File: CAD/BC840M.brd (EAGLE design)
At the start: 25.5 x 40 mm, 87 parts, among them J1 SM02B-SRSS-TB(LF)(SN), U2 BC840M, U3 LP5907MFX-3.3/NOPB, U4 LP5907MFX-3.3/NOPB, U5 ADS131M08IPBS, X1 ABM3B-8.000MHZ-B2-T, X2 FC-12M

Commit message: tweaks
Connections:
- new net VDDH: R2.2, R25.1, R28.1, R29.1, U2.A7
- net VDD: no longer R2.2, R25.1, R28.1, R29.1, U2.A7
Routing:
- net VDD: track 86.3 -> 46.3 mm
- net VDDH: track 0.00 -> 39.9 mm
- net GND: track 161.1 -> 165.6 mm
- net P113: track 22.0 -> 22.8 mm
- net CUR_DETECT: track 29.2 -> 28.3 mm
- net RESET: track 30.7 -> 30.0 mm

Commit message: Update BC840M.brd
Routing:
- net GND: track 165.6 -> 177.9 mm
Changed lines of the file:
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@@
 <wire x1="32.778640625" y1="48.306040625" x2="32.778640625" y2="47.652940625" width="0.1524" layer="16"/>
 <wire x1="32.778640625" y1="47.652940625" x2="35.054540625" y2="47.652940625" width="0.1524" layer="16"/>
+<wire x1="29.910021875" y1="42.274640625" x2="31.122721875" y2="43.487340625" width="0.1524" layer="16"/>
+<wire x1="31.122721875" y1="43.487340625" x2="32.699959375" y2="43.487340625" width="0.1524" layer="16"/>
+<wire x1="33.910021875" y1="44.674640625" x2="32.722721875" y2="43.487340625" width="0.1524" layer="16"/>
+<wire x1="32.722721875" y1="43.487340625" x2="32.699959375" y2="43.487340625" width="0.1524" layer="16"/>
+<wire x1="25.945503125" y1="31.252315625" x2="27.0635375" y2="31.252315625" width="0.1524" layer="16"/>
+<wire x1="20.3454" y1="31.7246" x2="21.2806375" y2="30.7893625" width="0.1524" layer="16"/>
+<wire x1="21.2806375" y1="30.7893625" x2="25.48255" y2="30.7893625" width="0.1524" layer="16"/>
+<wire x1="25.48255" y1="30.7893625" x2="25.945503125" y2="31.252315625" width="0.1524" layer="16"/>
 <wire x1="27.559" y1="60.2964" x2="27.559" y2="61.1092" width="0" layer="19" extent="1-1"/>
 <wire x1="28.3464" y1="60.2964" x2="28.3464" y2="59.509" width="0" layer="19" extent="1-1"/>
@@
 <wire x1="14.302740625" y1="34.2392" x2="15.76578125" y2="33.830259375" width="0" layer="19" extent="1-1"/>
 <wire x1="20.3454" y1="31.7246" x2="18.7208" y2="31.765859375" width="0" layer="19" extent="1-1"/>
-<wire x1="27.072778125" y1="32.0904625" x2="25.887778125" y2="32.731340625" width="0" layer="19" extent="1-1"/>
 <wire x1="28.072778125" y1="32.0904625" x2="27.072778125" y2="32.0904625" width="0" layer="19" extent="1-1"/>
 <wire x1="13.6118625" y1="35.699" x2="14.302740625" y2="34.2392" width="0" layer="19" extent="1-1"/>
@@
 <wire x1="28.724978125" y1="48.97120625" x2="31.278640625" y2="48.306040625" width="0" layer="19" extent="1-16"/>
 <wire x1="27.4828" y1="51.4269" x2="26.2609375" y2="49.2353625" width="0" layer="19" extent="1-1"/>
+<wire x1="35.676840625" y1="42.659178125" x2="33.910021875" y2="44.674640625" width="0" layer="19" extent="16-16"/>
 <wire x1="27.739459375" y1="55.83681875" x2="30.56901875" y2="56.3397375" width="0" layer="19" extent="1-16"/>
 <wire x1="26.9162625" y1="55.80888125" x2="27.739459375" y2="55.83681875" width="0" layer="19" extent="1-1"/>
 <wire x1="26.733378125" y1="54.480465625" x2="26.9162625" y2="55.80888125" width="0" layer="19" extent="1-1"/>
-<wire x1="32.699959375" y1="43.487340625" x2="29.910021875" y2="42.274640625" width="0" layer="19" extent="16-16"/>
-<wire x1="33.910021875" y1="44.674640625" x2="32.699959375" y2="43.487340625" width="0" layer="19" extent="16-16"/>
-<wire x1="35.676840625" y1="42.659178125" x2="33.910021875" y2="44.674640625" width="0" layer="19" extent="16-16"/>
 <wire x1="35.9156" y1="39.8018" x2="35.676840625" y2="42.659178125" width="0" layer="19" extent="16-16"/>
 <wire x1="34.2395" y1="39.237921875" x2="35.9156" y2="39.8018" width="0" layer="19" extent="1-1"/>

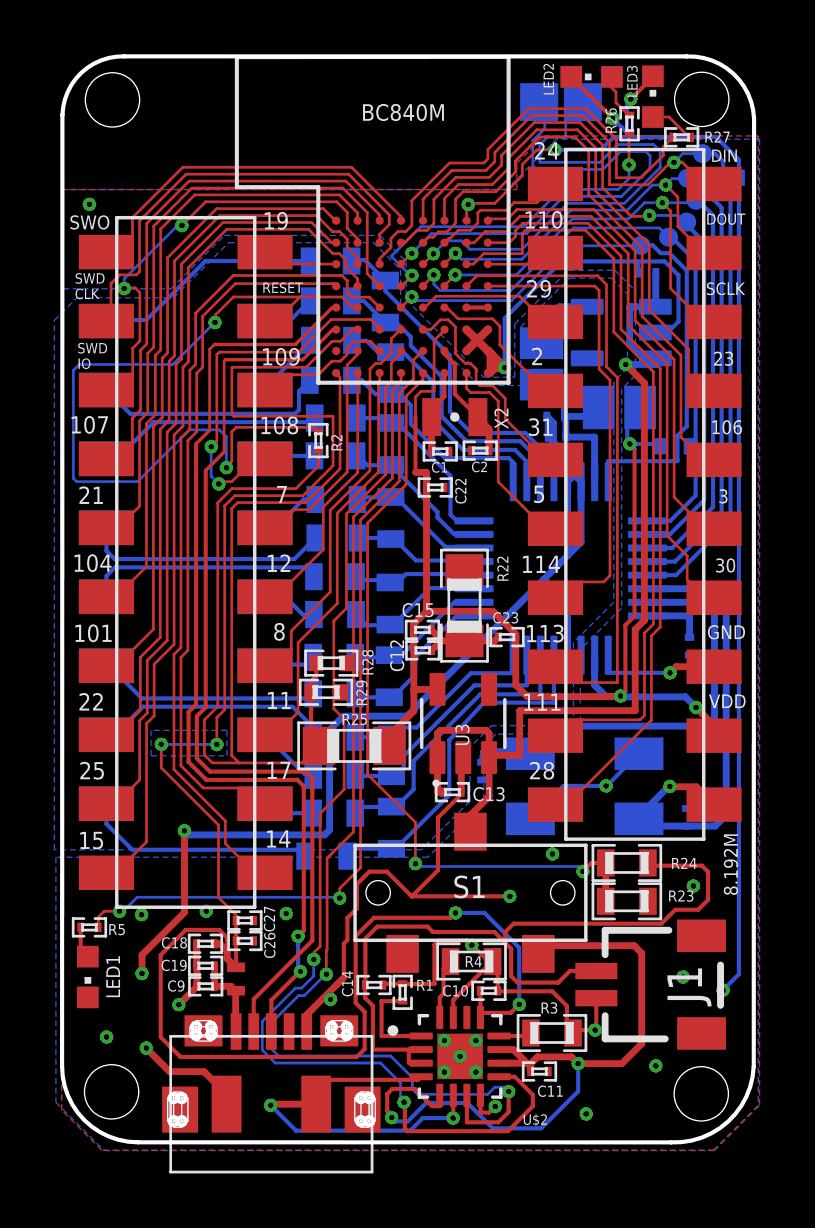
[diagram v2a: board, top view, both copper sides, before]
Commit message: added TVS diodes
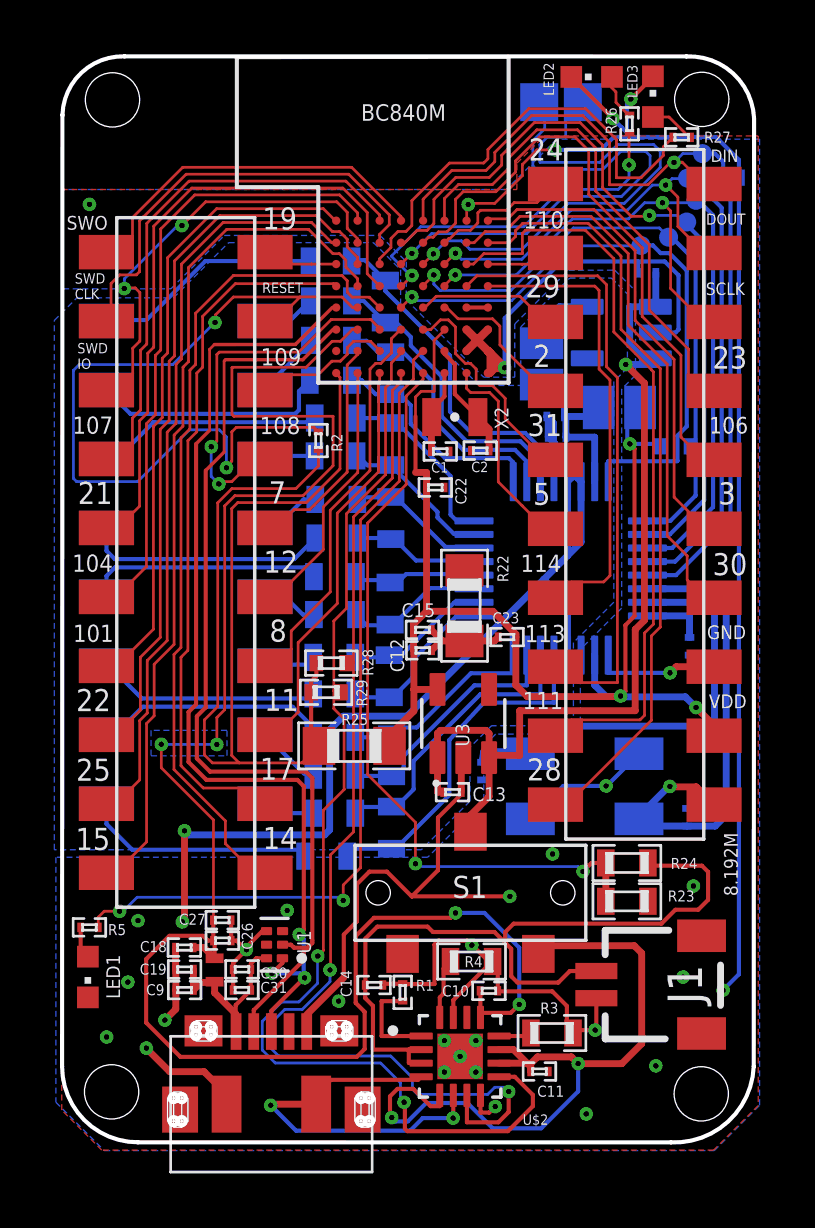
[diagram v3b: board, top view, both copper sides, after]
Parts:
- added C30: 0.1uF, standardparts:0201
- added C31: 10uF, standardparts:0201
- added U1: TPD4S012DRYR, TPD4S012DRYR:PSON50P145X100X60-6N
- moved U$3 0.85 mm to (18.3, 36.7)
- moved C27 0.83 mm to (18.6, 38.5)
- moved C26 0.83 mm to (18.6, 37.8)
- moved C9 0.79 mm to (17.2, 36.0)
- moved C18 0.79 mm to (17.2, 37.5)
- moved C19 0.79 mm to (17.2, 36.7)
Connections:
- net +5V: now also C30.2, C31.2, U1.6
- net D+: now also U1.1
- net D-: now also U1.2
- net GND: now also C30.1, C31.1, U1.4
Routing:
- net +5V: track 3.32 -> 6.76 mm
- net GND: track 177.9 -> 180.1 mm, vias 29 -> 30
- net D+: track 35.0 -> 37.1 mm, vias 2 -> 3
- net +5V_ISO: track 69.3 -> 67.7 mm
- net D-: track 34.4 -> 35.4 mm

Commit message: push
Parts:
- C16, C17, C20, C21, C24, C25, C28, C29: value 10pF -> 100pF
- R10, R11, R12, R13, R14, R15, R16, R17, R18, R19, R20, R21, R6, R7, R8, R9: value 10MOhm -> 1MOhm
- renumbered U$1 to U7, U$2 to U6, U$3 to I1

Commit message: latest
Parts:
- C15, C31: device standardparts:0201 -> standardparts:0402
- moved I1 0.62 mm to (17.7, 36.7)
- moved C9 0.56 mm to (16.6, 36.0)
- moved C18 0.56 mm to (16.6, 37.4)
- moved C19 0.55 mm to (16.6, 36.7)
- moved C30 0.53 mm to (18.9, 37.1)
- moved C12 0.39 mm to (25.6, 48.4)
- moved C31 0.37 mm to (19.0, 36.2)
- moved C15 0.33 mm to (25.6, 49.2)
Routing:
- net +5V: track 6.76 -> 7.82 mm
- net VDD: track 46.3 -> 47.2 mm

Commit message: edits and CAM
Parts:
- J1: value SM02B-SRSS-TB(LF)(SN) -> S2B-PH-SM4-TB(LF)(SN); device SM02B-SRSS-TB_LF__SN_:SM02B-SRSS-TB(LF)(SN) -> S2B-PH-SM4-TB_LF__SN_:JST_S2B-PH-SM4-TB(LF)(SN)
- moved R31 0.50 mm to (35.3, 55.5)
- moved SJ1 0.37 mm to (33.2, 57.1)
- moved I1 0.35 mm to (17.4, 37.0)
- moved C9 0.31 mm to (16.3, 36.0)
- moved C19 0.30 mm to (16.3, 36.7)
- moved C18 0.30 mm to (16.3, 37.4)
- moved C15 0.07 mm to (25.6, 49.3)
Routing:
- net VDD: track 47.2 -> 51.3 mm
- net GND: track 180.3 -> 182.8 mm
- net BAT: track 29.0 -> 31.4 mm
- net +5V: track 7.82 -> 8.64 mm
- net +5V_ISO: track 68.1 -> 68.7 mm

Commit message: fix
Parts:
- J1: value S2B-PH-SM4-TB(LF)(SN) -> SM02B-SRSS-TB(LF)(SN); device S2B-PH-SM4-TB_LF__SN_:JST_S2B-PH-SM4-TB(LF)(SN) -> SM02B-SRSS-TB_LF__SN_:SM02B-SRSS-TB(LF)(SN)
- moved J1 0.22 mm to (34.5, 36.1)
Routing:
- net BAT: track 31.4 -> 29.3 mm
- net GND: track 182.8 -> 181.0 mm
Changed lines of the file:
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@@
 <attribute name="VALUE" x="29.217515625" y="30.905684375" size="0.381" layer="27" rot="R180" align="top-left"/>
-</element>
-<element name="J1" library="S2B-PH-SM4-TB_LF__SN_" package="JST_S2B-PH-SM4-TB(LF)(SN)" value="S2B-PH-SM4-TB(LF)(SN)" x="34.3154" y="36.1696" smashed="yes" rot="R90">
-<attribute name="AVAILABILITY" value="In Stock" x="34.3154" y="36.1696" size="1.778" layer="27" rot="R90" display="off"/>
-<attribute name="DESCRIPTION" value=" Connector Header Surface Mount, Right Angle 2 position 0.079 (2.00mm) " x="34.3154" y="36.1696" size="1.778" layer="27" rot="R90" display="off"/>
-<attribute name="MF" value="JST Sales" x="34.3154" y="36.1696" size="1.778" layer="27" rot="R90" display="off"/>
-<attribute name="MP" value="S2B-PH-SM4-TB (LF)(SN)" x="34.3154" y="36.1696" size="1.778" layer="27" rot="R90" display="off"/>
-<attribute name="NAME" x="35.5953625" y="36.17834375" size="1.27315" layer="25" rot="R90" align="center"/>
-<attribute name="PACKAGE" value="None" x="34.3154" y="36.1696" size="1.778" layer="27" rot="R90" display="off"/>
-<attribute name="PRICE" value="None" x="34.3154" y="36.1696" size="1.778" layer="27" rot="R90" display="off"/>
-<attribute name="VALUE" x="37.632515625" y="35.9325375" size="0.4064" layer="27" rot="R270" align="center"/>
 </element>
 <element name="JP1" library="pinhead+" package="2X08_SMT" value="" x="17.2186625" y="51.7245625" smashed="yes" rot="MR90">
@@
 <attribute name="NAME" x="20.091390625" y="35.824153125" size="0.4064" layer="25" font="vector"/>
 <attribute name="VALUE" x="18.356575" y="35.298375" size="0.4064" layer="27" font="vector"/>
+</element>
+<element name="J1" library="SM02B-SRSS-TB_LF__SN_" package="SM02B-SRSS-TB(LF)(SN)" value="SM02B-SRSS-TB(LF)(SN)" x="34.533840625" y="36.14928125" smashed="yes" rot="R90">
+<attribute name="AVAILABILITY" value="In Stock" x="34.533840625" y="36.14928125" size="1.778" layer="27" rot="R90" display="off"/>
+<attribute name="DESCRIPTION" value=" Connector Header Surface Mount, Right Angle 2 position 0.039 (1.00mm) " x="34.533840625" y="36.14928125" size="1.778" layer="27" rot="R90" display="off"/>
+<attribute name="MF" value="JST Sales" x="34.533840625" y="36.14928125" size="1.778" layer="27" rot="R90" display="off"/>
+<attribute name="MP" value="SM02B-SRSS-TB(LF)(SN)" x="34.533840625" y="36.14928125" size="1.778" layer="27" rot="R90" display="off"/>
+<attribute name="NAME" x="34.924803125" y="35.802425" size="1.27315" layer="25" rot="R90" align="center"/>
+<attribute name="PACKAGE" value="None" x="34.533840625" y="36.14928125" size="1.778" layer="27" rot="R90" display="off"/>
+<attribute name="PRICE" value="None" x="34.533840625" y="36.14928125" size="1.778" layer="27" rot="R90" display="off"/>
+<attribute name="VALUE" x="34.925125" y="35.80214375" size="1.27416875" layer="27" rot="R90" align="center"/>
 </element>
 </elements>
@@
 <contactref element="U7" pad="MP1"/>
 <contactref element="U7" pad="MP2"/>
-<contactref element="J1" pad="1"/>
 <contactref element="R3" pad="1"/>
 <contactref element="R4" pad="1"/>
@@
 <wire x1="15.9945" y1="37.442134375" x2="15.9945" y2="36.7004625" width="0.254" layer="1"/>
 <wire x1="15.99704375" y1="36.69791875" x2="15.9945" y2="36.7004625" width="0.254" layer="1"/>
-<wire x1="15.981809375" y1="35.95115625" x2="16.29676875" y2="35.636196875" width="0.254" layer="1"/>
-<wire x1="16.29676875" y1="35.636196875" x2="16.29676875" y2="35.011246875" width="0.254" layer="1"/>
+<wire x1="16.29676875" y1="35.438075" x2="15.981809375" y2="35.753034375" width="0.254" layer="1"/>
+<wire x1="15.981809375" y1="35.95115625" x2="15.981809375" y2="35.753034375" width="0.254" layer="1"/>
+<wire x1="16.29676875" y1="35.438075" x2="16.29676875" y2="35.011246875" width="0.254" layer="1"/>
 <wire x1="16.446509375" y1="34.86150625" x2="16.29676875" y2="35.011246875" width="0.254" layer="1"/>
 <contactref element="U6" pad="15"/>
@@
 <wire x1="31.255003125" y1="35.38395625" x2="31.255003125" y2="34.61258125" width="0.1524" layer="1"/>
 <wire x1="31.4810625" y1="34.386521875" x2="31.255003125" y2="34.61258125" width="0.1524" layer="1"/>
-<wire x1="31.255003125" y1="35.38395625" x2="30.717340625" y2="35.92161875" width="0.1524" layer="1"/>
+<wire x1="31.255003125" y1="35.38395625" x2="31.164290625" y2="35.47466875" width="0.1524" layer="1"/>
+<wire x1="31.164290625" y1="35.47466875" x2="30.717340625" y2="35.92161875" width="0.1524" layer="1"/>
 <wire x1="31.4810625" y1="34.386521875" x2="31.587740625" y2="34.4932" width="0.1524" layer="1"/>
 <wire x1="31.587740625" y1="34.4932" x2="32.2961" y2="34.4932" width="0.1524" layer="1"/>
 <wire x1="32.2961" y1="34.4932" x2="32.3404" y2="34.5375" width="0.1524" layer="1"/>
-<wire x1="32.3404" y1="34.5375" x2="34.3154" y2="37.1696" width="0.1524" layer="1"/>
 <wire x1="28.963621875" y1="58.88989375" x2="28.963621875" y2="60.712190625" width="0.1524" layer="16"/>
 <wire x1="28.963621875" y1="60.712190625" x2="31.0580125" y2="62.80658125" width="0.1524" layer="16"/>
@@
 <wire x1="26.130334375" y1="49.283621875" x2="26.3437" y2="49.283621875" width="0.254" layer="1"/>
 <wire x1="26.413815625" y1="49.21350625" x2="26.413815625" y2="48.8269" width="0.254" layer="1"/>
+<contactref element="J1" pad="1"/>
+<wire x1="31.164290625" y1="35.47466875" x2="32.384228125" y2="35.47466875" width="0.1524" layer="1"/>
+<wire x1="32.384228125" y1="35.47466875" x2="32.558840625" y2="35.64928125" width="0.1524" layer="1"/>
 <wire x1="27.559" y1="60.2964" x2="27.559" y2="61.1092" width="0" layer="19" extent="1-1"/>
 <wire x1="28.3464" y1="60.2964" x2="28.3464" y2="59.509" width="0" layer="19" extent="1-1"/>
@@
 <wire x1="30.57131875" y1="32.9692" x2="28.61564375" y2="31.67634375" width="0" layer="19" extent="1-1"/>
 <wire x1="31.4810625" y1="34.386521875" x2="30.57131875" y2="32.9692" width="0" layer="19" extent="1-1"/>
-<wire x1="35.5346" y1="36.449" x2="34.3154" y2="37.1696" width="0" layer="19" extent="1-1"/>
-<wire x1="37.0078" y1="35.9664" x2="35.5346" y2="36.449" width="0" layer="19" extent="1-1"/>
 <wire x1="22.8473" y1="35.56" x2="24.477859375" y2="36.154359375" width="0" layer="19" extent="1-1"/>
 <wire x1="21.6708" y1="34.440859375" x2="22.8473" y2="35.56" width="0" layer="19" extent="1-1"/>
 <wire x1="28.125421875" y1="43.708440625" x2="27.3658375" y2="43.258740625" width="0" layer="19" extent="1-16"/>
-<wire x1="34.2395" y1="39.237921875" x2="34.3154" y2="37.1696" width="0" layer="19" extent="1-1"/>
-<wire x1="35.9156" y1="39.8018" x2="34.2395" y2="39.237921875" width="0" layer="19" extent="1-1"/>
 <wire x1="31.968440625" y1="31.4071" x2="30.57131875" y2="32.9692" width="0" layer="19" extent="1-1"/>
 <wire x1="30.72638125" y1="40.980359375" x2="29.15411875" y2="39.4208" width="0" layer="19" extent="1-1"/>
 <wire x1="29.910021875" y1="42.274640625" x2="30.72638125" y2="40.980359375" width="0" layer="19" extent="16-16"/>
-<wire x1="34.5313" y1="33.17748125" x2="32.2961" y2="34.4932" width="0" layer="19" extent="1-1"/>
+<wire x1="34.5313" y1="33.17748125" x2="32.3404" y2="34.5375" width="0" layer="19" extent="1-1"/>
 <wire x1="28.724978125" y1="48.97120625" x2="31.278640625" y2="48.306040625" width="0" layer="19" extent="1-16"/>
 <wire x1="27.4828" y1="51.4269" x2="26.130334375" y2="49.283621875" width="0" layer="19" extent="1-1"/>
@@
 <wire x1="26.9162625" y1="55.80888125" x2="27.739459375" y2="55.83681875" width="0" layer="19" extent="1-1"/>
 <wire x1="26.733378125" y1="54.480465625" x2="26.9162625" y2="55.80888125" width="0" layer="19" extent="1-1"/>
+<wire x1="35.9156" y1="39.8018" x2="35.676840625" y2="42.659178125" width="0" layer="19" extent="16-16"/>
+<wire x1="34.2395" y1="39.237921875" x2="35.9156" y2="39.8018" width="0" layer="19" extent="1-1"/>
+<wire x1="35.5346" y1="36.449" x2="32.558840625" y2="35.64928125" width="0" layer="19" extent="1-1"/>
+<wire x1="37.0078" y1="35.9664" x2="35.5346" y2="36.449" width="0" layer="19" extent="1-1"/>
 <wire x1="13.67028125" y1="64.907159375" x2="27.559" y2="64.3096" width="0" layer="19" extent="1-1"/>
 </signal>
@@
 <contactref element="C14" pad="2"/>
 <contactref element="U6" pad="2"/>
-<contactref element="J1" pad="2"/>
-<wire x1="34.3154" y1="35.1696" x2="31.3650375" y2="36.6696" width="0.1524" layer="1"/>
-<wire x1="31.3650375" y1="36.6696" x2="30.94085625" y2="36.24541875" width="0.1524" layer="1"/>
+<wire x1="30.94085625" y1="36.24541875" x2="31.3650375" y2="36.6696" width="0.1524" layer="1"/>
 <wire x1="30.94085625" y1="36.24541875" x2="29.436440625" y2="36.24541875" width="0.1524" layer="1"/>
 <wire x1="29.436440625" y1="36.24541875" x2="29.20491875" y2="36.476940625" width="0.1524" layer="1"/>
@@
 <wire x1="26.124053125" y1="38.305740625" x2="26.32201875" y2="38.107775" width="0.1524" layer="1"/>
 <wire x1="24.274778125" y1="38.305740625" x2="26.124053125" y2="38.305740625" width="0.1524" layer="1"/>
+<contactref element="J1" pad="2"/>
+<wire x1="31.3650375" y1="36.6696" x2="32.538521875" y2="36.6696" width="0.1524" layer="1"/>
+<wire x1="32.538521875" y1="36.6696" x2="32.558840625" y2="36.64928125" width="0.1524" layer="1"/>
 </signal>
 <signal name="0PIN">

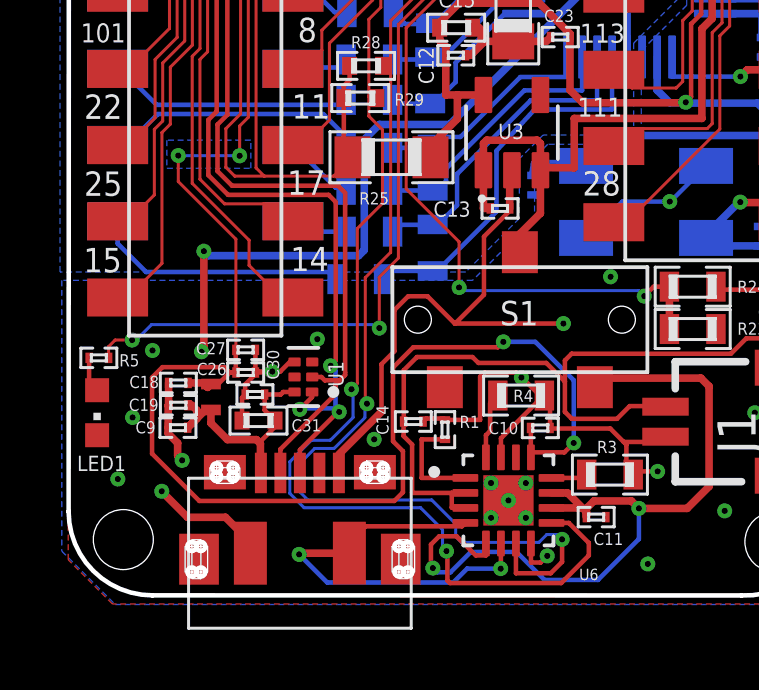
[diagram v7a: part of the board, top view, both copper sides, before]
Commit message: fix holes for microusb
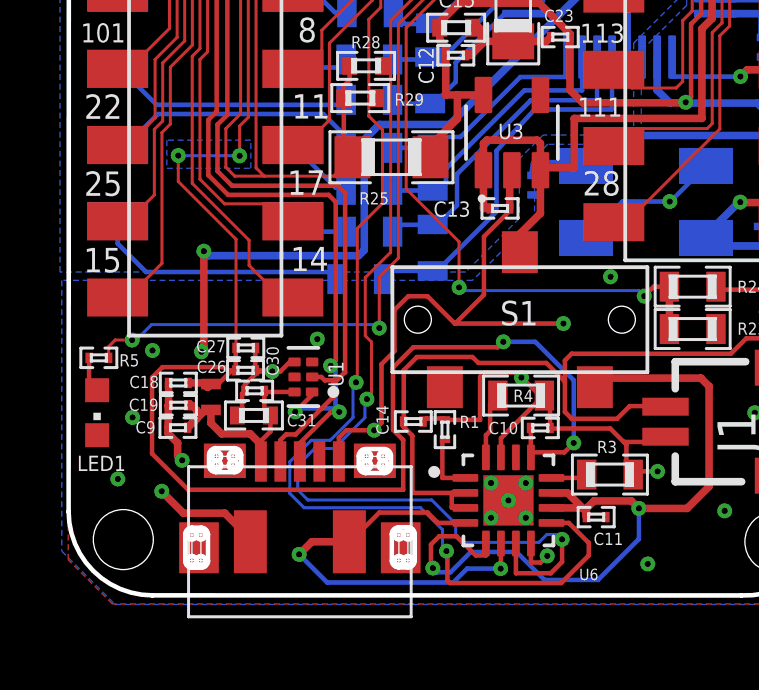
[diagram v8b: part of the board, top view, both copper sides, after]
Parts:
- moved U7 0.38 mm to (20.4, 33.3)
- moved C31 0.23 mm to (18.8, 36.4)
- moved C30 0.12 mm to (18.9, 37.2)
- moved C26 0.07 mm to (18.6, 37.9)
- moved C27 0.07 mm to (18.6, 38.6)
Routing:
- net TS: track 3.52 -> 2.14 mm
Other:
- outline, holes or cut-outs redrawn
